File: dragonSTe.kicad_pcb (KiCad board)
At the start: 2 copper layers, 293 parts, among them J2 MIDI OUT, J3 MIDI IN, J4 DB25_Socket, J5 DB25_Pins, J6 Keyboard, J7 Internal FDD, SW1 RESET, U1 68000, U30 LF347DT, U32 LF347DT, U33 LM78L82, U34 LMC1992, U37 DMA, U38 WD1772, U39 STB, U40 GST_SHIFTER, U42 GST_MCU, U5 LM555xM, U7 MC6850, U8 MC6850, U9 YM2149, X1 8.010613MHz

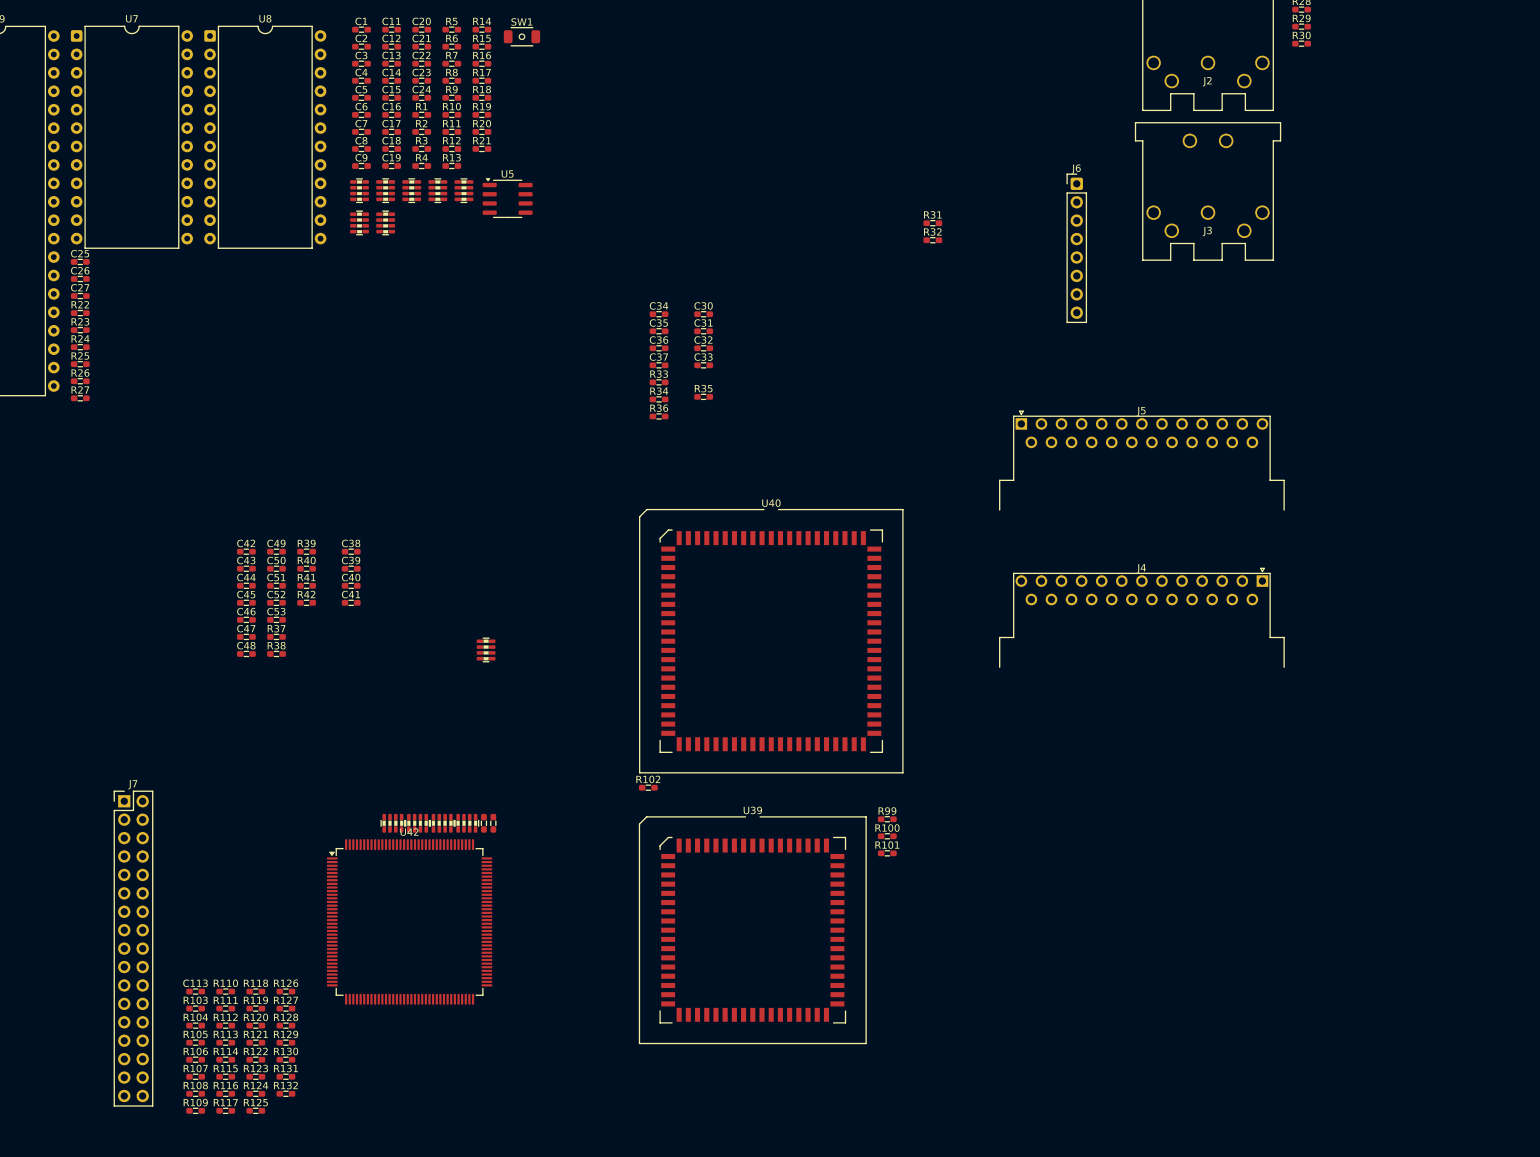
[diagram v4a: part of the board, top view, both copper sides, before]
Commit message: motherboard: More signal routing, and starting in on the BoM
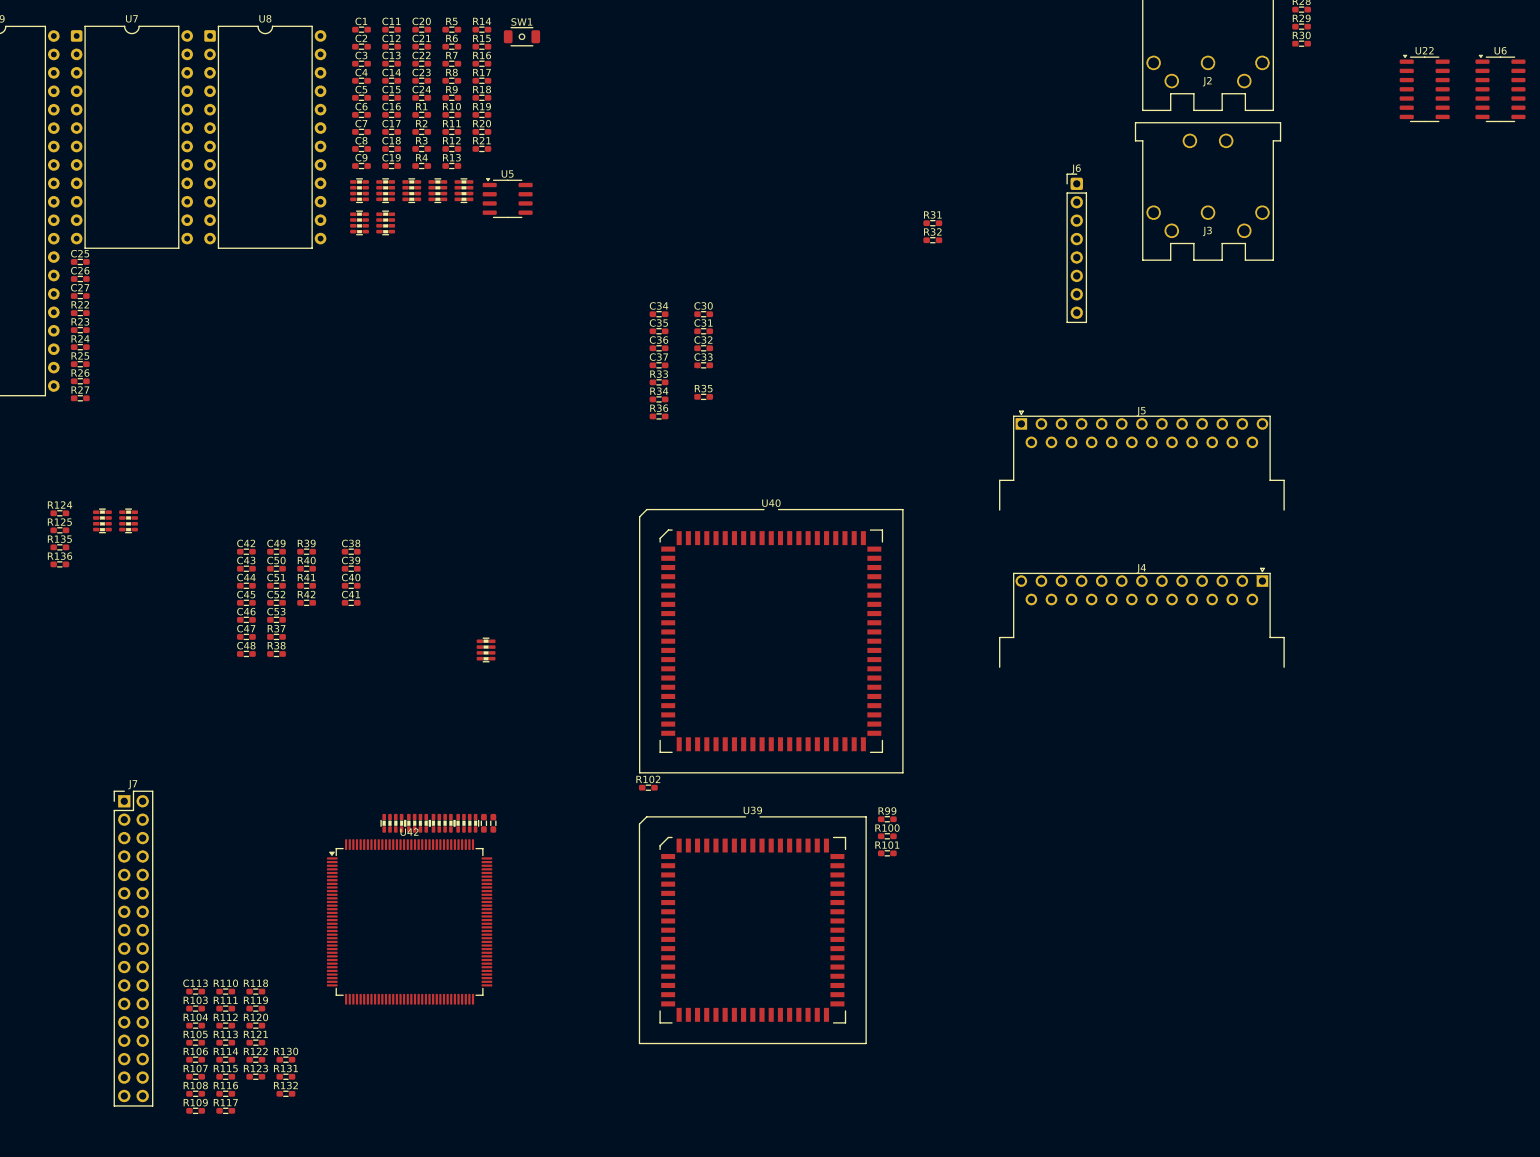
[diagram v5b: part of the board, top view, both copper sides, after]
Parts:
- removed R126, R127, R128, R129: 75R, rhais_rcl:R0603
- added R135: 1k, rhais_rcl:R0603, F.Cu at (189.8, 122.3)
- added R136: 10k, rhais_rcl:R0603, F.Cu at (189.8, 124.7)
- added RN26: 10k, rhais_rcl:R0603_Array_Concave_4, F.Cu at (195.7, 118.7)
- added RN27: 10k, rhais_rcl:R0603_Array_Concave_4, F.Cu at (199.2, 118.7)
- added U22: 74LS05, Package_SO:SO-14_3.9x8.65mm_P1.27mm, F.Cu at (378.0, 59.2)
- added U6: 74LS05, Package_SO:SO-14_3.9x8.65mm_P1.27mm, F.Cu at (388.4, 59.2)
- R124: value 75R -> 100R
- R125: value 75R -> 150R
- moved R125 84.5 mm to (189.8, 120.0)
- moved R124 84.5 mm to (189.8, 117.7)
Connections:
- net /Video/RAM.A0 renamed /RAM/RAM.A0
- net /Video/RAM.A1 renamed /RAM/RAM.A1
- net /Video/RAM.A2 renamed /RAM/RAM.A2
- net /Video/RAM.A3 renamed /RAM/RAM.A3
- net /Video/RAM.A4 renamed /RAM/RAM.A4
- net /Video/RAM.A5 renamed /RAM/RAM.A5
- net /Video/RAM.A6 renamed /RAM/RAM.A6
- net /Video/RAM.A7 renamed /RAM/RAM.A7
- net /Video/RAM.A8 renamed /RAM/RAM.A8
- net /Video/RAM.A9 renamed /RAM/RAM.A9
- net /Video/RAM.D0 renamed /RAM/RAM.D0
- net /Video/RAM.D1 renamed /RAM/RAM.D1
- net /Video/RAM.D10 renamed /RAM/RAM.D10
- net /Video/RAM.D11 renamed /RAM/RAM.D11
- net /Video/RAM.D12 renamed /RAM/RAM.D12
- net /Video/RAM.D13 renamed /RAM/RAM.D13
- net /Video/RAM.D14 renamed /RAM/RAM.D14
- net /Video/RAM.D15 renamed /RAM/RAM.D15
- net /Video/RAM.D2 renamed /RAM/RAM.D2
- net /Video/RAM.D3 renamed /RAM/RAM.D3
- net /Video/RAM.D4 renamed /RAM/RAM.D4
- net /Video/RAM.D5 renamed /RAM/RAM.D5
- net /Video/RAM.D6 renamed /RAM/RAM.D6
- net /Video/RAM.D7 renamed /RAM/RAM.D7
- net /Video/RAM.D8 renamed /RAM/RAM.D8
- net /Video/RAM.D9 renamed /RAM/RAM.D9
- net /Video/RAM.~{CASH0} renamed /RAM/RAM.~{CASH0}
- net /Video/RAM.~{CASH1} renamed /RAM/RAM.~{CASH1}
- net /Video/RAM.~{CASL0} renamed /RAM/RAM.~{CASL0}
- net /Video/RAM.~{CASL1} renamed /RAM/RAM.~{CASL1}
- net /Video/RAM.~{RAS0} renamed /RAM/RAM.~{RAS0}
- net /Video/RAM.~{RAS1} renamed /RAM/RAM.~{RAS1}
- net /Video/RAM.~{WE} renamed /RAM/RAM.~{WE}
- net /Video/~{DISK_INT} renamed /IO Interfaces/~{DISK_INT}
- net /Video/~{IACK} renamed /IO Interfaces/~{IACK}
- net /Video/~{MFP_CS} renamed /IO Interfaces/~{MFP_CS}
- net /Video/~{PAD0X} renamed /DAC + Joysticks/~{PAD0X}
- net /Video/~{PAD0Y} renamed /DAC + Joysticks/~{PAD0Y}
- net /Video/~{PAD1X} renamed /DAC + Joysticks/~{PAD1X}
- net /Video/~{PAD1Y} renamed /DAC + Joysticks/~{PAD1Y}
- net /Video/~{SND_INT} renamed /IO Interfaces/~{SND_INT}
- R122 pad 1: Net-(Q8-PadE) -> Net-(Q7-PadE)
- R122 pad 2: /Video/R -> unconnected-(R122-Pad2)
- R123 pad 1: GND -> Net-(Q6-PadE)
- R123 pad 2: /Video/R -> unconnected-(R123-Pad2)
- R124 pad 1: Net-(Q7-PadE) -> Net-(Q10-PadE)
- R125 pad 1: Net-(Q7-PadE) -> GND
- R125 pad 2: /Video/G -> Net-(Q10-PadE)
- U42 pad 135: /Video/RDY -> /Disk & Floppy/RDY
- U42 pad 136: /Video/~{FCS} -> /Disk & Floppy/~{FCS}
- U42 pad 137: unconnected-(U42-~{PEN}-Pad137) -> /DAC + Joysticks/~{PEN}
- U42 pad 15: /Video/~{HD_INT} -> /Disk & Floppy/~{HD_INT}
- U42 pad 16: /Video/FD_INT -> /Disk & Floppy/FD_INT
- U42 pad 18: /Video/SND_DIR -> /IO Interfaces/SND_DIR
- U42 pad 19: /Video/SND_CS -> /IO Interfaces/SND_CS
- U42 pad 23: /Video/~{BUS_ERR} -> /CPU+ROMs/~{BUS_ERR}
- U42 pad 24: unconnected-(U42-~{VMA}-Pad24) -> /Video/~{VMA}
- U42 pad 26: /Video/~{BGK} -> /CPU+ROMs/~{BGK}
- U42 pad 28: /Video/~{BLT_BG} -> /CPU+ROMs/~{BLT_BG}
- U42 pad 29: /Video/~{BR} -> /CPU+ROMs/~{BR}
- U42 pad 33: /Video/~{IPL0} -> /CPU+ROMs/~{IPL0}
- U42 pad 34: /Video/~{IPL1} -> /CPU+ROMs/~{IPL1}
- U42 pad 35: /Video/~{IPL2} -> /CPU+ROMs/~{IPL2}
- U42 pad 38: /Video/FC2 -> /CPU+ROMs/FC2
- U42 pad 39: /Video/FC1 -> /CPU+ROMs/FC1
- U42 pad 40: /Video/FC0 -> /CPU+ROMs/FC0
- U42 pad 48: /Video/N6850 -> /IO Interfaces/N6850
- U42 pad 60: /Video/~{BLT_INT} -> /CPU+ROMs/~{BLT_INT}
- U42 pad 66: /Video/~{RESET} -> /CPU+ROMs/~{RESET}
- U42 pad 93: /Video/~{MFP_INT} -> /IO Interfaces/~{MFP_INT}
- U42 pad 98: unconnected-(U42-~{PADRST}-Pad98) -> /DAC + Joysticks/~{PAD_RESET}

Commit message: motherboard: Begun routing the internal floppy disk interface
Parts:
- J7: footprint Connector_PinHeader_2.54mm:PinHeader_2x17_P2.54mm_Vertical -> rhais_connector-pinheader:PinHeader_2x17_P2.54mm_Vertical
- U22, U30, U32, U6: footprint Package_SO:SO-14_3.9x8.65mm_P1.27mm -> rhais_package-smd:SO-14_3.9x8.65mm_P1.27mm
- U37: footprint Package_DIP:DIP-40_W15.24mm_Socket -> rhais_package-dip:DIP-40_W15.24mm_Socket
- U38: footprint Package_DIP:DIP-28_W15.24mm_Socket -> rhais_package-dip:DIP-28_W15.24mm_Socket
- U5: footprint Package_SO:SOIC-8_3.9x4.9mm_P1.27mm -> rhais_package-smd:SO-8_3.9x4.9mm_P1.27mm
- U9: footprint Package_DIP:DIP-40_W15.24mm -> rhais_package-dip:DIP-40_W15.24mm_Socket
- moved R89 265.9 mm to (373.7, 200.2), turned to -90 degrees
- moved R93 253.8 mm to (365.4, 222.7)
- moved R94 253.7 mm to (365.4, 194.8)
- moved R91 253.3 mm to (365.4, 197.3)
- moved R92 253.3 mm to (365.4, 199.8)
- moved R97 249.2 mm to (365.4, 210.0), turned to 180 degrees
- moved R96 249.2 mm to (365.4, 204.9), turned to 180 degrees
- moved R95 249.2 mm to (365.4, 202.4), turned to 180 degrees
- moved R98 249.2 mm to (365.4, 207.4), turned to 180 degrees
- moved C112 244.0 mm to (350.7, 226.5)
- moved U38 236.7 mm to (340.0, 210.0)
- moved U37 233.7 mm to (316.0, 217.6)
- moved R87 224.2 mm to (330.0, 235.8), turned to -90 degrees
- moved C111 218.9 mm to (326.8, 193.5)
- moved R90 214.7 mm to (326.8, 198.6), turned to 180 degrees
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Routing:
- net Net-(U37-HDRQ): track 0.00 -> 62.2 mm, vias 0 -> 2
- net /Disk & Floppy/~{RDATA}: track 0.00 -> 42.6 mm
- net /Disk & Floppy/~{INDEX}: track 0.00 -> 29.4 mm, vias 0 -> 1
- net Net-(U38-DIRC): track 0.00 -> 24.9 mm
- net Net-(U38-STEP): track 0.00 -> 23.7 mm
- net /Disk & Floppy/~{WP}: track 0.00 -> 23.6 mm
- net Net-(U38-MO): track 0.00 -> 23.5 mm
- net Net-(U38-WG): track 0.00 -> 18.1 mm, vias 0 -> 1
- net /Disk & Floppy/~{MO}: track 0.00 -> 16.9 mm
- net /Disk & Floppy/~{HDRQ}: track 0.00 -> 13.9 mm
- net +5V: track 0.00 -> 13.9 mm, vias 0 -> 8
- net Net-(R95-Pad2): track 0.00 -> 10.8 mm
- net Net-(R98-Pad2): track 0.00 -> 10.8 mm
- net Net-(R96-Pad2): track 0.00 -> 10.8 mm
- net Net-(U38-WD): track 0.00 -> 9.75 mm, vias 0 -> 2
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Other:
- copper layers 2 -> 4

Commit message: motherboard: Begun routing the FM synth sound chip
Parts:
- added U13: 74LS04, rhais_package-smd:SO-14_3.9x8.65mm_P1.27mm, F.Cu at (259.9, 146.3)
- added U45: 74LS04, rhais_package-smd:SO-14_3.9x8.65mm_P1.27mm, F.Cu at (276.6, 41.5)
- moved J4 243.5 mm to (128.7, 38.6), turned to 180 degrees
- moved R33 149.9 mm to (134.2, 41.5), turned to 90 degrees
- moved C25 72.7 mm to (125.8, 54.2), turned to 90 degrees
- moved R22 63.3 mm to (130.9, 75.8), turned to -90 degrees
- moved U9 27.1 mm to (150.0, 65.0), turned to 90 degrees
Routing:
- net Net-(U9-IOB0): track 0.00 -> 35.2 mm
- net Net-(U9-IOB1): track 0.00 -> 35.1 mm
- net Net-(U9-IOB2): track 0.00 -> 35.0 mm
- net Net-(U9-IOB3): track 0.00 -> 34.9 mm
- net Net-(U9-IOA5): track 0.00 -> 34.9 mm
- net Net-(U9-IOB4): track 0.00 -> 34.8 mm
- net Net-(U9-IOB5): track 0.00 -> 34.7 mm
- net Net-(U9-IOB6): track 0.00 -> 34.6 mm
- net Net-(U9-IOB7): track 0.00 -> 34.5 mm
- net /DAC + Joysticks/AUDIOS: track 0.00 -> 20.1 mm
- net +5V: track 13.9 -> 17.1 mm, vias 8 -> 9
- net Net-(U10-IO0): track 0.00 -> 2.05 mm
- net GND: track 4.35 -> 6.20 mm, vias 4 -> 6

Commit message: motherboard: Routed one of the parallel interfaces and the ROMs
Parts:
- added Q1: 2N3904, rhais_package-smd:SOT-23, F.Cu at (218.6, 54.9)
- added Q10: 2N3904, rhais_package-smd:SOT-23, F.Cu at (211.1, 74.3)
- added Q2: 2N3904, rhais_package-smd:SOT-23, F.Cu at (218.6, 59.8)
- added Q3: 2N3904, rhais_package-smd:SOT-23, F.Cu at (218.6, 64.6)
- added Q4: 2N3904, rhais_package-smd:SOT-23, F.Cu at (218.6, 69.5)
- added Q5: 2N3904, rhais_package-smd:SOT-23, F.Cu at (218.6, 74.3)
- added Q6: 2N3904, rhais_package-smd:SOT-23, F.Cu at (211.1, 54.9)
- added Q7: 2N3904, rhais_package-smd:SOT-23, F.Cu at (211.1, 59.8)
- added Q8: 2N3904, rhais_package-smd:SOT-23, F.Cu at (211.1, 64.6)
- added Q9: 2N3904, rhais_package-smd:SOT-23, F.Cu at (211.1, 69.5)
- added U10: MC68901, Package_DIP:DIP-48_W15.24mm_Socket, F.Cu at (170.8, 97.6)
- added U2: 27C010, rhais_package-dip:DIP-32_W15.24mm_Socket, F.Cu at (100.0, 188.4)
- added U3: 27C010, rhais_package-dip:DIP-32_W15.24mm_Socket, F.Cu at (100.0, 170.0)
- U7, U8: footprint Package_DIP:DIP-24_W15.24mm -> rhais_package-dip:DIP-24_W15.24mm_Socket
- moved R26 148.5 mm to (326.5, 35.4), turned to -90 degrees
- moved R25 145.2 mm to (324.0, 35.4), turned to -90 degrees
- moved R23 138.6 mm to (322.6, 44.2), turned to -90 degrees
- moved R27 138.4 mm to (314.0, 35.4), turned to -90 degrees
- moved R24 137.0 mm to (320.0, 44.2), turned to -90 degrees
- moved U7 127.1 mm to (315.0, 84.4), turned to -90 degrees
- moved J5 122.5 mm to (219.6, 38.6), turned to 180 degrees
- moved C26 108.6 mm to (297.9, 58.4), turned to 180 degrees
- moved C27 105.8 mm to (297.9, 76.8), turned to 180 degrees
- moved U8 105.5 mm to (315.0, 66.0), turned to -90 degrees
- moved C6 82.6 mm to (311.9, 44.5), turned to 90 degrees
- moved C7 81.9 mm to (310.6, 44.5), turned to 90 degrees
- moved C5 79.5 mm to (302.4, 24.4), turned to -90 degrees
- moved U1 77.1 mm to (139.4, 118.7), turned to -90 degrees
- moved R1 74.5 mm to (303.6, 24.4), turned to 90 degrees
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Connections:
- U5 pad 1: unconnected-(U5-GND-Pad1) -> GND
- U5 pad 8: unconnected-(U5-VCC-Pad8) -> +5V
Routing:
- net /CPU+ROMs/~{RESET}: track 0.00 -> 61.7 mm, vias 0 -> 1
- net /CPU+ROMs/SysBus.A2: track 0.00 -> 38.9 mm
- net /CPU+ROMs/SysBus.A1: track 0.00 -> 38.9 mm
- net /CPU+ROMs/SysBus.A17: track 0.00 -> 38.9 mm
- net Net-(D1-A): track 0.00 -> 35.0 mm
- net /IO Interfaces/TX_KBD: track 0.00 -> 33.8 mm
- net /IO Interfaces/RX_MIDI_OUT: track 0.00 -> 29.2 mm
- net /IO Interfaces/500kHz: track 0.00 -> 29.0 mm
- net /IO Interfaces/SER_IRQ: track 0.00 -> 21.7 mm
- net /IO Interfaces/RX_KBD: track 0.00 -> 21.2 mm
- net /CPU+ROMs/SysBus.A6: track 0.00 -> 19.5 mm
- net /CPU+ROMs/SysBus.A14: track 0.00 -> 19.5 mm
- net /CPU+ROMs/SysBus.A11: track 0.00 -> 19.5 mm
- net /CPU+ROMs/SysBus.D8: track 0.00 -> 19.5 mm
- net /CPU+ROMs/SysBus.D13: track 0.00 -> 19.5 mm
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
